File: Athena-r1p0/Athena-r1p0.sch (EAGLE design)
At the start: 78 parts, among them J1-NEST-OWL1 CONN_12X2, J2-USB MF-CON-MICROUSB-RIGHT, J3-MK22-DBG FEMALE 2x3, J4 MF-CON-2.54mm-01x14, J5 MF-CON-2.54mm-01x14, SW1 MF-SW-TACT-4.2MM, SW2 MF-SW-TACT-4.2MM, U1 NCP1117-VREG-5V0, U2 RT9080-33GJ5, U3 RT9080-18GJ5, U4 MCP73831/2, U5 FE310, U6 32MBit, U7 MK22FN128VLH10, X1 JST 2-Pin, Y1 TSX-3225-16.0000MF18X-AC0, Y2 SIT1533AI-H4-DCC-32.768E

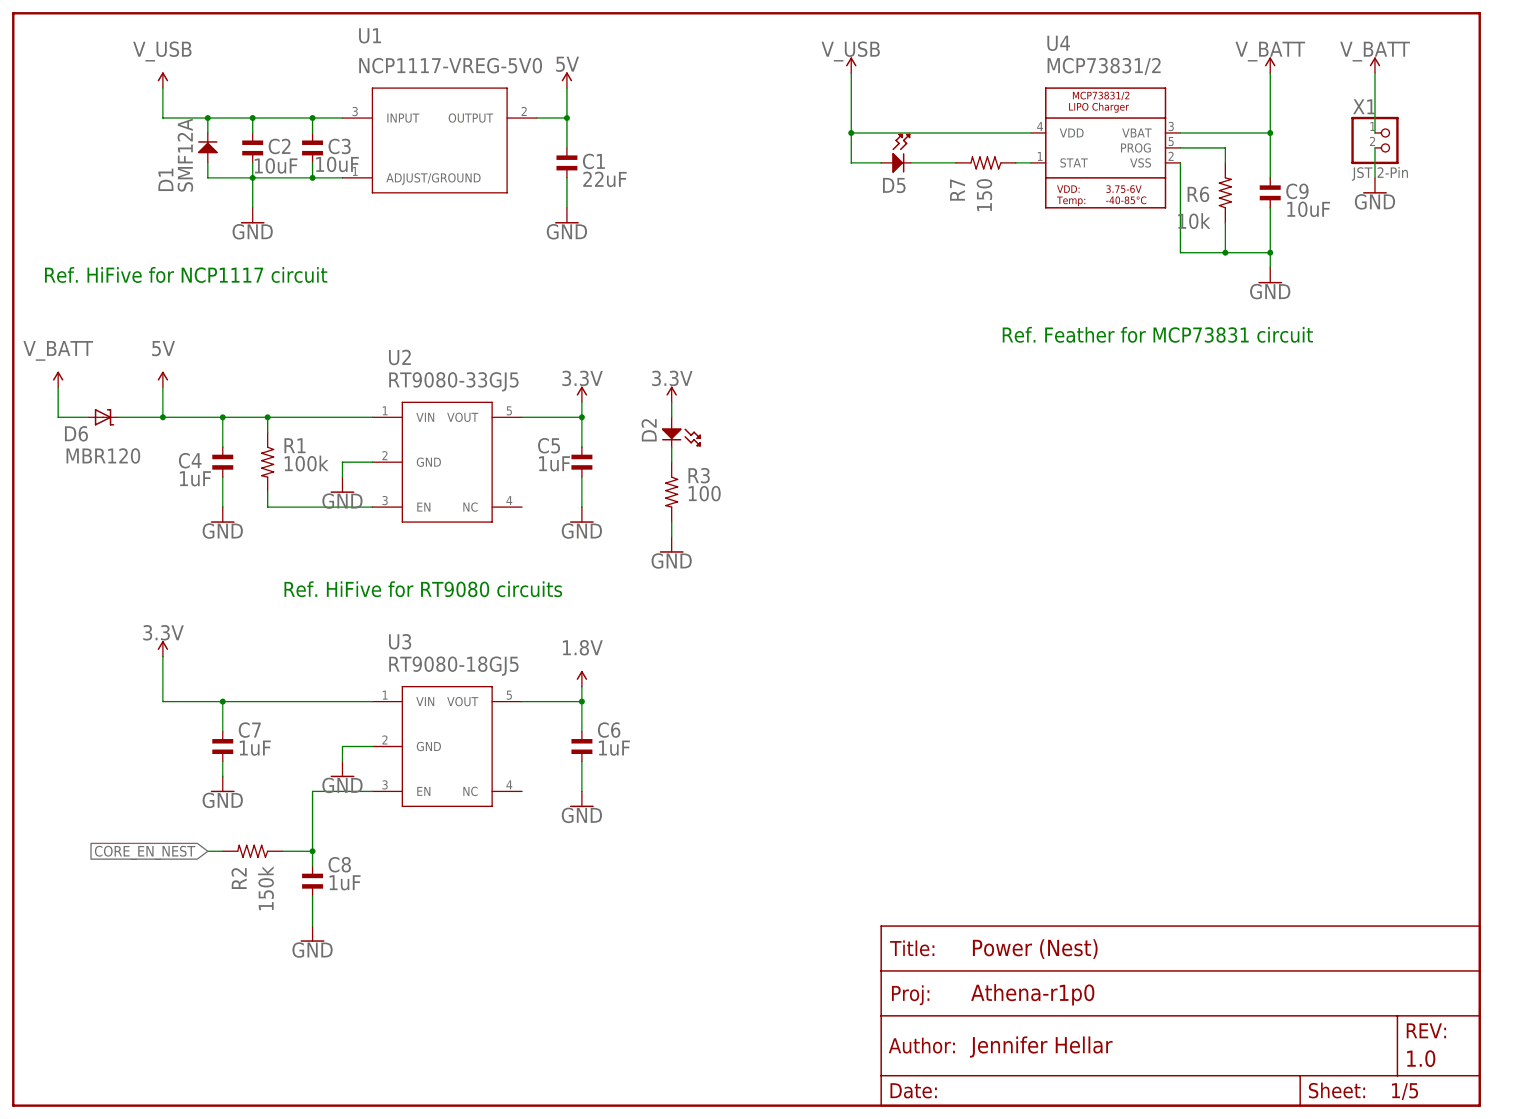
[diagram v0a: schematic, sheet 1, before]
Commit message: Continued work on addressing Erik's comments, specifically, removing the NCP1117.  Also changed out the TVS diodes to the devices in the HiFive design.
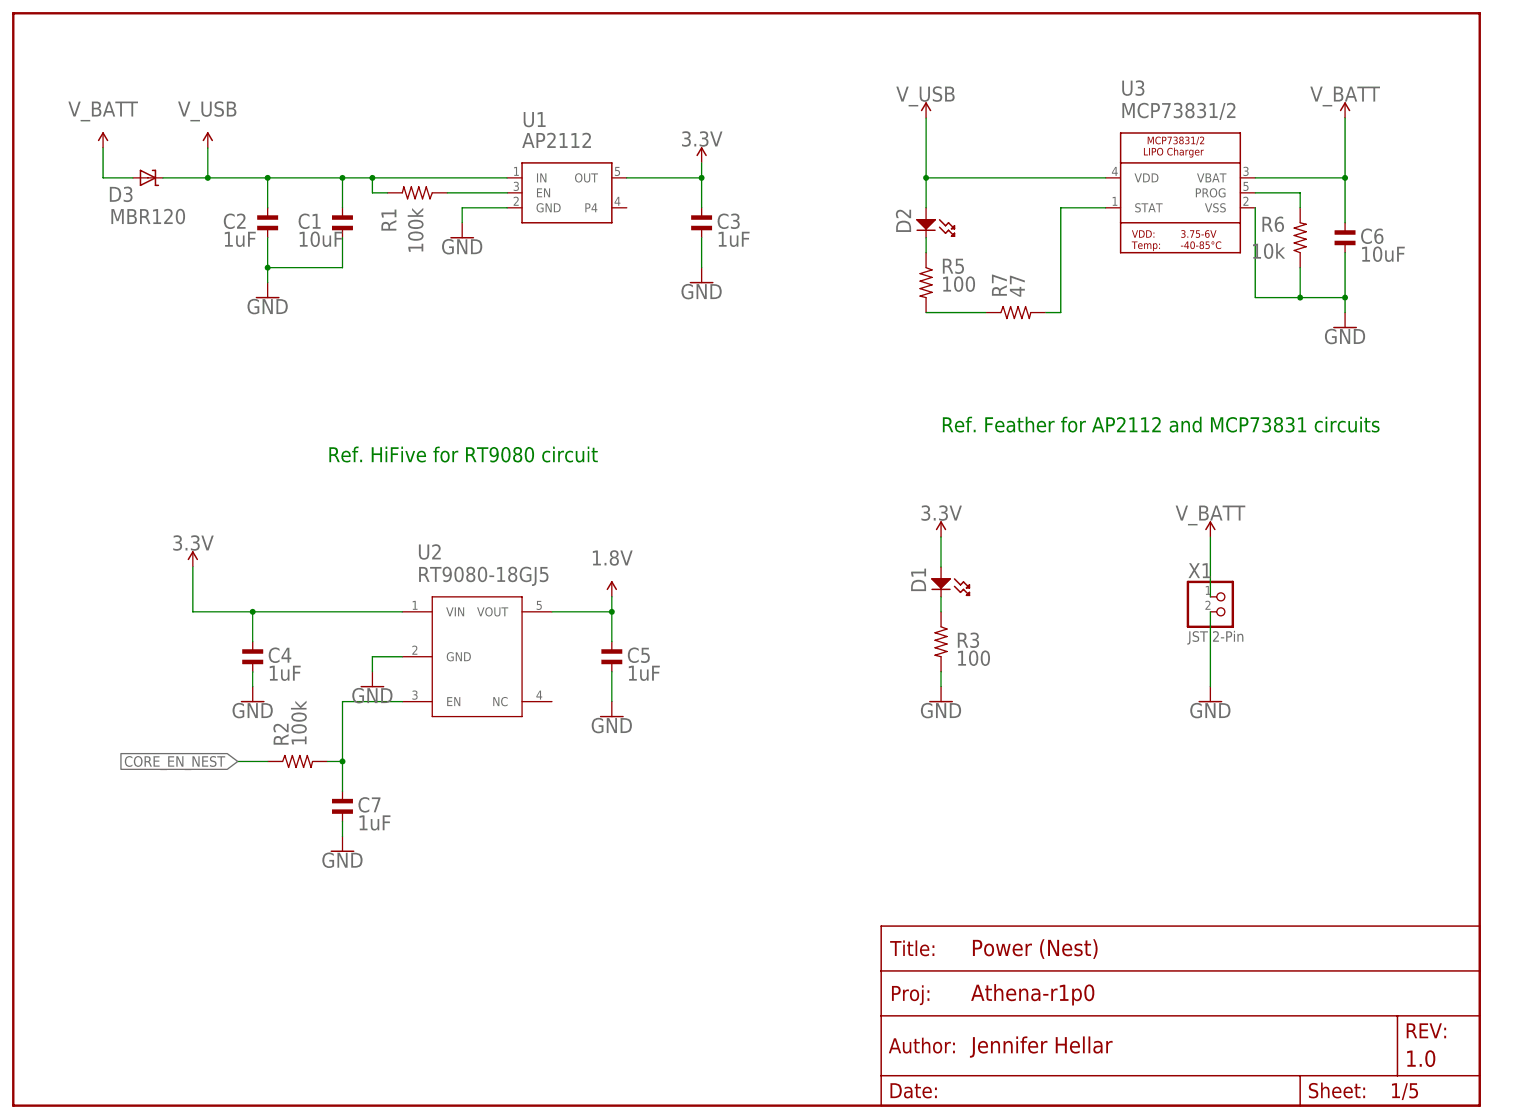
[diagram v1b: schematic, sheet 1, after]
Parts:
- removed C29, C30: 0.1uF, MF_Passives:CAPACITOR_NP_0603
- removed D6: MBR120, Athena-r0p1:DIODE-SCHOTTKYSOD-123
- removed D7, D8: 24V, SparkFun RED-V RedBoard:SPARKFUN-DISCRETESEMI_DIODE_TVS
- removed D9: 1N4148WT-7, Athena-r0p1:1N4148WT-7
- removed J1-NEST-OWL1: CONN_12X2, SparkFun-Connectors:CONN_12X2
- removed U4: MCP73831/2, Athena-r0p1:IC_POWER_LIPO_MCP73831/2
- added D3: MBR120, Athena-r0p1:DIODE-SCHOTTKYSOD-123
- added D4: 24V, Athena-r0p1:PESD0603-240TVS0603
- added J1: (no value), SparkFun-Connectors:CONN_08X2
- added R5: 100, MF_Passives:RESISTOR_0402
- C1: value 22uF -> 10uF
- C10: value 0.1uF -> 10nF
- C2, C3: value 10uF -> 1uF; device MF_Passives:CAPACITOR_NP_0603 -> MF_Passives:CAPACITOR_NP_0402
- C27, C28, C4, C5, C7: device MF_Passives:CAPACITOR_NP_0603 -> MF_Passives:CAPACITOR_NP_0402
- C6: value 1uF -> 10uF
- C8: value 1uF -> 0.1uF; device MF_Passives:CAPACITOR_NP_0603 -> MF_Passives:CAPACITOR_NP_0402
- C9: value 10uF -> 0.1uF; device MF_Passives:CAPACITOR_NP_0603 -> MF_Passives:CAPACITOR_NP_0402
- D1: value SMF12A -> MF-LED-0603-GREEN; device Athena-r0p1:SMF12A -> MF_LEDs:LED_SINGLE-0603-GREEN
- D2: value MF-LED-0603-GREEN -> MF-LED-0603-RED; device MF_LEDs:LED_SINGLE-0603-GREEN -> MF_LEDs:LED_SINGLE-0603-RED
- D5: value MF-LED-0603-RED -> 24V; device MF_LEDs:LED_SINGLE-0603-RED -> Athena-r0p1:PESD0603-240TVS0603
- R1, R13, R14, R15, R16, R3, R6: device MF_Passives:RESISTOR_0603 -> MF_Passives:RESISTOR_0402
- R2: value 150k -> 100k; device MF_Passives:RESISTOR_0603 -> MF_Passives:RESISTOR_0402
- R7: value 150 -> 47; device MF_Passives:RESISTOR_0603 -> MF_Passives:RESISTOR_0402
- U1: value NCP1117-VREG-5V0 -> AP2112; device Athena-r0p1:NCP1117LPST50T3G -> Athena-r0p1:AP2112
- U2: value RT9080-33GJ5 -> RT9080-18GJ5; device Athena-r0p1:RT9080-33GJ5 -> Athena-r0p1:RT9080-18GJ5
- U3: value RT9080-18GJ5 -> MCP73831/2; device Athena-r0p1:RT9080-18GJ5 -> Athena-r0p1:IC_POWER_LIPO_MCP73831/2
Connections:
- removed net 5V: C1.P$1, C4.P$1, D6.C, J1-NEST-OWL1.3, J1-NEST-OWL1.4, J4.PIN1, R1.P$1, U1.OUTPUT, U2.VIN
- removed net N$8 (its old number): D5.CATHODE, R7.P$2
- new net N$1: R1.P$1, U1.EN
- new net N$5: R5.P$2, R7.P$1
- net 1.8V: now also C5.P$1, U2.VOUT; no longer C6.P$1, J1-NEST-OWL1.7, J1-NEST-OWL1.8, U3.VOUT
- net 3.3V: now also C3.P$1, C4.P$1, C8.P$1, C9.P$1, D1.ANODE, U1.OUT, U2.VIN; no longer C29.P$1, C30.P$1, C5.P$1, C7.P$1, D2.ANODE, D9.CATHODE, J1-NEST-OWL1.5, J1-NEST-OWL1.6, U2.VOUT, U3.VIN
- net CORE_EN_NEST: now also J1.16, R2.P$1; no longer J1-NEST-OWL1.24, R2.P$2
- net GND: now also D4.A, D5.A, U1.GND, U3.VSS; no longer C29.P$2, C30.P$2, D1.ANODE, D7.A, D8.A, J1-NEST-OWL1.1, J1-NEST-OWL1.2, U1.ADJUST/GROUND, U3.GND, U4.VSS
- net JTAG_TCK: now also J1.7; no longer J1-NEST-OWL1.15
- net JTAG_TCK_NEST: now also J1.8; no longer J1-NEST-OWL1.16
- net JTAG_TDI: now also J1.11; no longer J1-NEST-OWL1.19
- net JTAG_TDI_NEST: now also J1.12; no longer J1-NEST-OWL1.20
- net JTAG_TDO: now also J1.9; no longer J1-NEST-OWL1.17
- net JTAG_TDO_NEST: now also J1.10; no longer J1-NEST-OWL1.18
- net JTAG_TMS: now also J1.5; no longer J1-NEST-OWL1.13
- net JTAG_TMS_NEST: now also J1.6; no longer J1-NEST-OWL1.14
- net N$2: now also D1.CATHODE; no longer D2.CATHODE
- net N$3: now also D2.CATHODE, R5.P$1; no longer R1.P$2, U2.EN
- net N$4: now also C7.P$1, R2.P$2, U2.EN; no longer C8.P$1, R2.P$1, U3.EN
- net N$6: now also R7.P$2, U3.STAT; no longer R7.P$1, U4.STAT
- net N$7: now also U3.PROG; no longer U4.PROG
- net RESET: now also D5.C, J1.13; no longer D8.C, D9.ANODE, J1-NEST-OWL1.21
- net RESET_NEST: now also J1.14; no longer J1-NEST-OWL1.22
- net UART_RX: now also J1.3; no longer J1-NEST-OWL1.11
- net UART_RX_NEST: now also J1.2; no longer J1-NEST-OWL1.10
- net UART_TX: now also J1.1; no longer J1-NEST-OWL1.9
- net UART_TX_NEST: now also J1.4; no longer J1-NEST-OWL1.12
- net VDD_CORE_EN: now also J1.15; no longer J1-NEST-OWL1.23
- net V_BATT: now also C6.P$1, D3.A, U3.VBAT; no longer C9.P$1, D6.A, U4.VBAT
- net V_USB: now also C1.P$1, D2.ANODE, D3.C, J4.PIN1, R1.P$2, U1.IN, U3.VDD; no longer C3.P$1, D1.CATHODE, D5.ANODE, U1.INPUT, U4.VDD
- net WAKE: now also D4.C; no longer D7.C
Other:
- note added: "Ref. Feather for AP2112 and MCP73831 circuits"
- note added: "Ref. HiFive for RT9080 circuit"
- note removed: "Is one pin sufficient for transferring pwr from nest to owl? Or should we double up 3.3V and 1.8V and GND pins to have a stronger connection?"
- note removed: "Ref. Feather for MCP73831 circuit"
- note removed: "Ref. HiFive for NCP1117 circuit"
- note removed: "Ref. HiFive for RT9080 circuits"
- moved on the sheet: C1, C2, C27, C28, C3, C4, C5, C6, C7, D2, R1, R12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

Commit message: Implementing changes suggested by Erik and Ashish during July schematic review
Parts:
- removed C23, C24, C25, C26: 10uF, MF_Passives:CAPACITOR_NP_0603
- removed J2-USB: MF-CON-MICROUSB-RIGHT, MF_Connectors:USB_MICRO_RIGHT
- removed J3-MK22-DBG: FEMALE 2x3, SparkFun-Connectors:CONN_03X2FEMALE
- added C30, C32, C35, C36, C37: 0.1uF, MF_Passives:CAPACITOR_NP_0402
- added FRAME6: FRAME-LETTER, Athena-r0p1:FRAME-LETTER
- added J2: (no value), SparkFun-Connectors:CONN_08X2
- added J3: TC2050-IDC-NL, Athena-r0p1:TC2050-IDC-NL
- added J6: MF-CON-2.54mm-01x14, MF_Connectors:CON_01X14_PTH_2.54MM
- added R18: DNP, MF_Passives:RESISTOR_0402
- added R19, R20: 100k, MF_Passives:RESISTOR_0402
- added R21: 0, MF_Passives:RESISTOR_0402
- added TP1, TP2, TP3, TP4: TEST-POINT3X5, Athena-r0p1:TEST-POINT3X5
- added U4: PRTR5V0U2X,215, Athena-r0p1:PRTR5V0U2X,215
- C13, C14, C15, C21: value 0.1uF -> 10uF; device MF_Passives:CAPACITOR_NP_0603 -> MF_Passives:CAPACITOR_NP_0402
- C17: value 10uF -> DNP
- C22: device MF_Passives:CAPACITOR_NP_0603 -> MF_Passives:CAPACITOR_NP_0402
- FRAME3: SHEETNM OWL-TO-NEST HEADER -> OFF-BOARD-DEBUG HEADER
- FRAME5: SHEETNM Headers (Owl) -> Oscillators and Memory (Owl)
- J1: value (none) -> MF-CON-MICROUSB-RIGHT; device SparkFun-Connectors:CONN_08X2 -> MF_Connectors:USB_MICRO_RIGHT
- J4: value MF-CON-2.54mm-01x14 -> TC2030-IDC-NL; device MF_Connectors:CON_01X14_PTH_2.54MM -> Athena-r0p1:TC2030-IDC-NL
- R3, R5: value 100 -> 1k
- R7: value 47 -> DNP
- Y2: value SIT1533AI-H4-DCC-32.768E -> KX3211A0032.768000; device Athena-r0p1:SIT1533AI-H4-DCC-32.768E -> Athena-r0p1:KX3211A0032.768000
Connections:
- removed net CORE_EN_NEST: J1.16, R2.P$1
- removed net N$5 (its old number): R5.P$2, R7.P$1
- new net BATT_VOLT: J6.PIN4, R19.P$2, R20.P$1
- new net N$7: R21.P$1, U5.AON_PSD_LFCLKSEL
- new net P35: TP1.1, U7.PTB0/LLWU_P5
- new net P36: TP2.1, U7.PTB1
- new net P37: TP3.1, U7.PTB2
- new net P38: TP4.1, U7.PTB3
- new net VOLT_BAT: C1.P$2, C10.P$2, C11.P$2, C12.P$2, C13.P$2, C14.P$2, C15.P$2, C18.P$2, C19.P$2, C2.P$2, C20.P$2, C21.P$2, C22.P$2, C27.P$2, C28.P$2, C3.P$2, C30.P$2, C31.P$2, C32.P$2, C33.P$2, C34.P$2, C35.P$2, C36.P$2, C37.P$2, C4.P$2, C5.P$2, C6.P$2, C7.P$2, C8.P$2, C9.P$2, D4.A, D5.A, J1.GND, J1.SLD, J2.15, J2.16, J3.10, J3.7, J3.8, J3.9, J4.5, R18.P$1, R20.P$2, R21.P$2, R3.P$2, R6.P$1, SW1.P$1, SW1.P$2, SW2.P$1, SW2.P$2, U1.GND, U2.GND, U3.VSS, U4.GND/1, U5.GND, U6.GND, U7.GND, U7.VREFL, U7.VSSA, X1.2, Y1.2, Y1.4, Y2.GND
- net 16MHZ_IN: now also Y1.IN; no longer Y1.1
- net 16MHZ_OUT: now also Y1.OUT; no longer Y1.3
- net 3.3V: now also C30.P$1, C32.P$1, C35.P$1, C36.P$1, C37.P$1, J3.6, J4.1, J5.PIN2, J6.PIN14, R7.P$2, Y2.EN; no longer C23.P$1, C24.P$1, C25.P$1, C26.P$1, J3-MK22-DBG.1, J4.PIN14, J4.PIN2
- net 32KHZ_CLK: now also Y2.OUT; no longer Y2.CLK_OUT
- net CS0: now also J5.PIN4; no longer J4.PIN4
- net CS2: now also J5.PIN8; no longer J4.PIN8
- net CS3: now also J5.PIN9; no longer J4.PIN9
- net DBG_RESET: now also J4.3; no longer J3-MK22-DBG.3
- net DBG_SWDCLK: now also J4.4; no longer J3-MK22-DBG.4
- net DBG_SWDIO: now also J4.2; no longer J3-MK22-DBG.2
- net DBG_SWO: now also J4.6; no longer J3-MK22-DBG.6
- net GND: now also J5.PIN3, J6.PIN13; no longer C1.P$2, C10.P$2, C11.P$2, C12.P$2, C13.P$2, C14.P$2, C15.P$2, C18.P$2, C19.P$2, C2.P$2, C20.P$2, C21.P$2, C22.P$2, C23.P$2, C24.P$2, C25.P$2, C26.P$2, C27.P$2, C28.P$2, C3.P$2, C31.P$2, C33.P$2, C34.P$2, C4.P$2, C5.P$2, C6.P$2, C7.P$2, C8.P$2, C9.P$2, D4.A, D5.A, J2-USB.GND, J2-USB.SLD, J3-MK22-DBG.5, J4.PIN13, J4.PIN3, J5.PIN4, R3.P$2, R6.P$1, SW1.P$1, SW1.P$2, SW2.P$1, SW2.P$2, U1.GND, U2.GND, U3.VSS, U5.AON_PSD_LFCLKSEL, U5.GND, U6.GND, U7.GND, U7.VREFL, U7.VSSA, X1.2, Y1.2, Y1.4, Y2.GND
- net IO11: now also J5.PIN10; no longer J4.PIN10
- net IO19: now also J6.PIN7; no longer J5.PIN7
- net IO20: now also J6.PIN8; no longer J5.PIN8
- net IO21: now also J6.PIN9; no longer J5.PIN9
- net IO22: now also J6.PIN10; no longer J5.PIN10
- net JTAG_TCK: now also J2.7, J3.4; no longer J1.7
- net JTAG_TCK_NEST: now also J2.8; no longer J1.8
- net JTAG_TDI: now also J2.11, J3.2; no longer J1.11
- net JTAG_TDI_NEST: now also J2.12; no longer J1.12
- net JTAG_TDO: now also J2.9, J3.3; no longer J1.9
- net JTAG_TDO_NEST: now also J2.10; no longer J1.10
- net JTAG_TMS: now also J2.5, J3.5; no longer J1.5
- net JTAG_TMS_NEST: now also J2.6; no longer J1.6
- net MISO: now also J5.PIN6; no longer J4.PIN6
- net MOSI: now also J5.PIN5; no longer J4.PIN5
- net N$4: now also R18.P$2, R7.P$1
- net N$6: now also R5.P$2; no longer R7.P$2
- net PWM0_0: now also J6.PIN5; no longer J5.PIN5
- net PWM0_1: now also J6.PIN6; no longer J5.PIN6
- net RESET: now also J2.13, J3.1, J6.PIN1; no longer J1.13, J5.PIN1
- net RESET_NEST: now also J2.14; no longer J1.14
- net RXI: now also J6.PIN12; no longer J5.PIN12
- net SCK: now also J5.PIN7; no longer J4.PIN7
- net SCL: now also J5.PIN12; no longer J4.PIN12
- net SDA: now also J5.PIN11; no longer J4.PIN11
- net TXO: now also J6.PIN11; no longer J5.PIN11
- net UART_RX: now also J2.3; no longer J1.3
- net UART_RX_NEST: now also J2.2; no longer J1.2
- net UART_TX: now also J2.1; no longer J1.1
- net UART_TX_NEST: now also J2.4; no longer J1.4
- net USB_N: now also J1.D-, U4.3; no longer J2-USB.D-
- net USB_P: now also J1.D+, U4.2; no longer J2-USB.D+
- net VDD_CORE_EN: now also J6.PIN3, R2.P$1; no longer J1.15, J5.PIN3
- net V_BATT: now also R19.P$1
- net V_USB: now also J1.5V, J5.PIN1, U4.VDD/4; no longer J2-USB.5V, J4.PIN1
- net WAKE: now also J6.PIN2; no longer J5.PIN2
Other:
- note added: "16MHz TSX-3225 Oscillator"
- note added: "32MBit Flash Memory"
- note added: "32kHz KX3211 Oscillator"
- note added: "BATT Charge LED (red)"
- note added: "DNP Resistor Pads for optional pullup/down on RT9080 EN pin"
- note added: "ESD protection for USB data lines"
- note added: "J1 Bridge connector notes Default: Closed (1->2, 3->4, ..., 15->16) to program/debug on-board (Athena) FE310. Open and access NEST-side pins to program/debug off-board FE310 using Athena MK22 controller."
- note added: "J2 Bridge for on/off-board FE310 Debug, J3 10pin Tag-Connect for on-board FE310 Debug"
- note added: "J4 6pin Tag-Connect, MK22 Debug"
- note added: "LiPo Batt Connector configured for RC battery polarity (not Adafruit/Sparkfun polarity)"
- note added: "MK22 Processor (USB/JTAG/UART controller)"
- note added: "Main Processor: FE310"
- note added: "PWR LED (green)"
- note added: "Power & Filtering"
- note added: "Power pin capacitors"
- note added: "RX/TX labels corr. to FE310 persp."
- note added: "RX/TX labels match FE310 datasheet"
- note added: "RX/TX_NEST labels consistent with MK22 datasheet"
- note added: "RX/TX_NEST labels corr. to MK22 persp."
- note added: "Ref. Feather for MCP73831 circuit"
- note added: "USB & Battery Charging"
- note removed: "Ref. Feather for AP2112 and MCP73831 circuits"
